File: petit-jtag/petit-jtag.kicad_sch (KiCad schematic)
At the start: 9 parts, among them CON101 JTAG-2X3-1.27MM-HDR, CON102 USB-B1HSB6, CON103 JTAG-2X5-HDR-SHROUD, CON104 HDR1X3, U101 AZ1117CH-3.3TRG1

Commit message: mostly done v1.0
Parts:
- logo101: footprint db-artwork:db-logo_10mm -> db-artwork:db-logo_7.5mm
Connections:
- net +3V3: now also CON103.4 (Vcc)
- net VCC: no longer CON103.4 (Vcc)
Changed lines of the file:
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@@
   (junction (at 221.615 81.28) (diameter 0) (color 0 0 0 0)
   )
-  (junction (at 224.155 73.66) (diameter 0) (color 0 0 0 0)
-  )
   (junction (at 92.075 95.25) (diameter 0) (color 0 0 0 0)
   )
@@
     (stroke (width 0) (type default))
   )
-  (wire (pts (xy 224.155 94.615) (xy 224.155 73.66))
-    (stroke (width 0) (type default))
-  )
   (wire (pts (xy 190.5 102.235) (xy 198.755 102.235))
     (stroke (width 0) (type default))
@@
     (stroke (width 0) (type default))
   )
-  (wire (pts (xy 224.155 73.66) (xy 225.425 73.66))
+  (wire (pts (xy 217.805 73.66) (xy 225.425 73.66))
     (stroke (width 0) (type default))
   )
@@
   )
   (wire (pts (xy 221.615 97.155) (xy 221.615 81.28))
-    (stroke (width 0) (type default))
-  )
-  (wire (pts (xy 217.805 73.66) (xy 224.155 73.66))
     (stroke (width 0) (type default))
   )
@@
     (effects (font (size 1.27 1.27)) (justify left bottom))
   )
-  (symbol (lib_id "power:+3V3") (at 129.54 70.485 0) (unit 1)
-    (in_bom yes) (on_board yes) (dnp no) (fields_autoplaced)
-    (property "Reference" "#PWR0102" (at 129.54 74.295 0)
-      (effects (font (size 1.27 1.27)) hide)
-    )
-    (property "Value" "+3V3" (at 129.54 66.04 0)
-      (effects (font (size 1.27 1.27)))
-    )
-    (property "Footprint" "" (at 129.54 70.485 0)
-      (effects (font (size 1.27 1.27)) hide)
-    )
-    (property "Datasheet" "" (at 129.54 70.485 0)
+  (symbol (lib_id "power:+3V3") (at 225.425 73.66 270) (unit 1)
+    (in_bom yes) (on_board yes) (dnp no) (fields_autoplaced)
+    (property "Reference" "#PWR0102" (at 221.615 73.66 0)
+      (effects (font (size 1.27 1.27)) hide)
+    )
+    (property "Value" "+3V3" (at 228.6 73.66 90)
+      (effects (font (size 1.27 1.27)) (justify left))
+    )
+    (property "Footprint" "" (at 225.425 73.66 0)
+      (effects (font (size 1.27 1.27)) hide)
+    )
+    (property "Datasheet" "" (at 225.425 73.66 0)
       (effects (font (size 1.27 1.27)) hide)
     )
@@
       (effects (font (size 1.524 1.524)) (justify left))
     )
-    (property "Footprint" "db-artwork:db-logo_10mm" (at 182.245 156.845 0)
+    (property "Footprint" "db-artwork:db-logo_7.5mm" (at 182.245 156.845 0)
       (effects (font (size 1.524 1.524)) hide)
     )
@@
         (path "/9bb394b8-bc21-4e2d-a33d-3ebd944f79a1"
           (reference "CON104") (unit 1)
+        )
+      )
+    )
+  )
+  (symbol (lib_id "power:+3V3") (at 129.54 70.485 0) (unit 1)
+    (in_bom yes) (on_board yes) (dnp no) (fields_autoplaced)
+    (property "Reference" "#PWR0108" (at 129.54 74.295 0)
+      (effects (font (size 1.27 1.27)) hide)
+    )
+    (property "Value" "+3V3" (at 129.54 66.04 0)
+      (effects (font (size 1.27 1.27)))
+    )
+    (property "Footprint" "" (at 129.54 70.485 0)
+      (effects (font (size 1.27 1.27)) hide)
+    )
+    (property "Datasheet" "" (at 129.54 70.485 0)
+      (effects (font (size 1.27 1.27)) hide)
+    )
+    (pin "1")
+    (instances
+      (project "petit-jtag"
+        (path "/9bb394b8-bc21-4e2d-a33d-3ebd944f79a1"
+          (reference "#PWR0108") (unit 1)
         )
       )
@@
     )
   )
-  (symbol (lib_id "power:VCC") (at 225.425 73.66 270) (unit 1)
-    (in_bom yes) (on_board yes) (dnp no) (fields_autoplaced)
-    (property "Reference" "#PWR0106" (at 221.615 73.66 0)
-      (effects (font (size 1.27 1.27)) hide)
-    )
-    (property "Value" "VCC" (at 228.6 73.66 90)
-      (effects (font (size 1.27 1.27)) (justify left))
-    )
-    (property "Footprint" "" (at 225.425 73.66 0)
-      (effects (font (size 1.27 1.27)) hide)
-    )
-    (property "Datasheet" "" (at 225.425 73.66 0)
-      (effects (font (size 1.27 1.27)) hide)
-    )
+  (symbol (lib_id "power:VCC") (at 224.155 94.615 270) (unit 1)
+    (in_bom yes) (on_board yes) (dnp no) (fields_autoplaced)
+    (property "Reference" "#PWR0106" (at 220.345 94.615 0)
+      (effects (font (size 1.27 1.27)) hide)
+    )
+    (property "Value" "VCC" (at 227.33 94.615 90)
+      (effects (font (size 1.27 1.27)) (justify left))
+    )
+    (property "Footprint" "" (at 224.155 94.615 0)
+      (effects (font (size 1.27 1.27)) hide)
+    )
+    (property "Datasheet" "" (at 224.155 94.615 0)
+      (effects (font (size 1.27 1.27)) hide)
+    )

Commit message: version 1.0 ready
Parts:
- added CON105: HDR1X2, db-thparts:HDR1X2, symbol db-connectors:HDR1X2
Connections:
- net +5V: now also CON105.1
- net GND: now also CON105.2

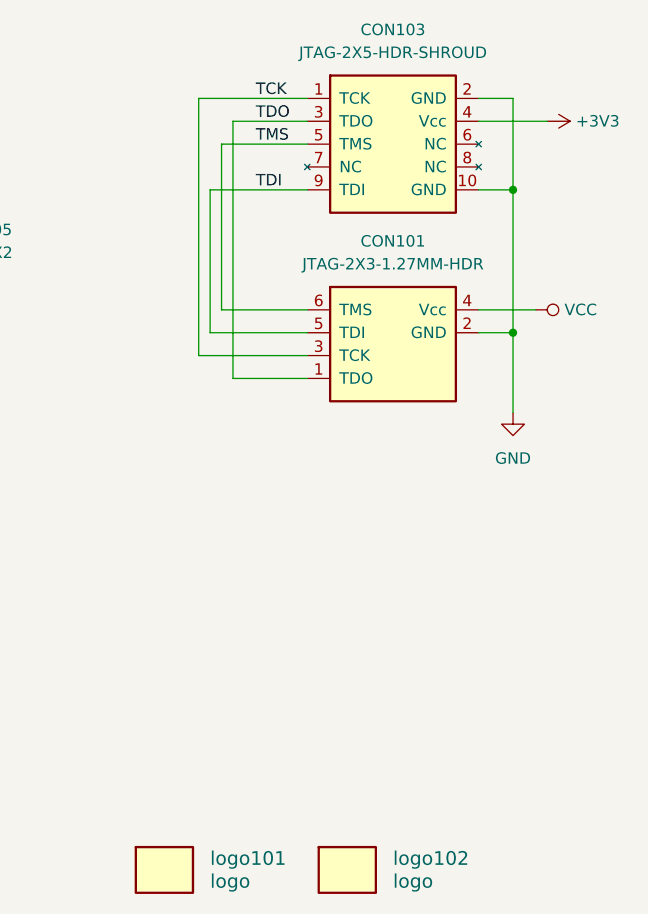
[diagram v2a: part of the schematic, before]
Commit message: updated with new staggered pin headers instead of 2x3
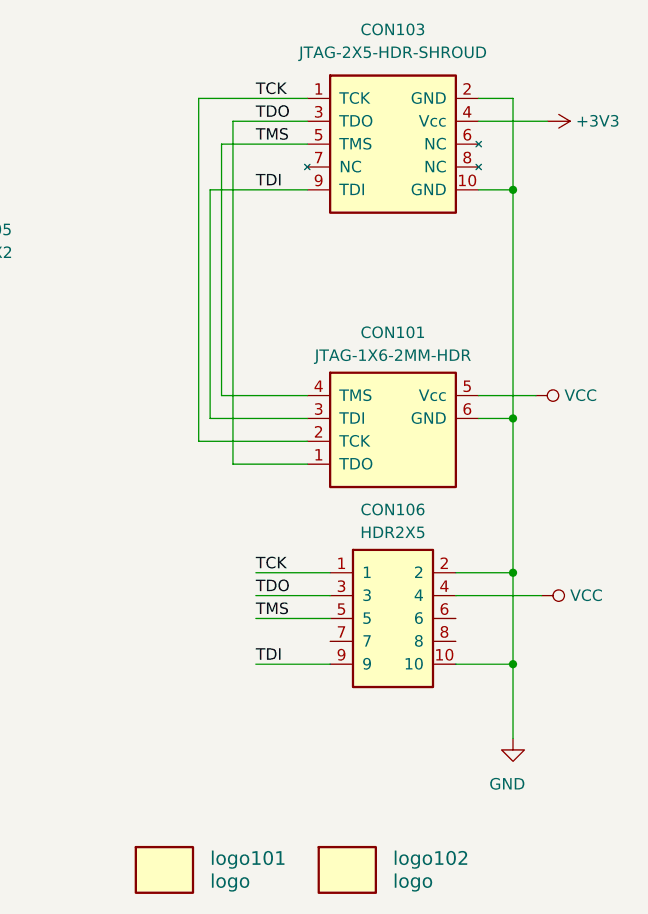
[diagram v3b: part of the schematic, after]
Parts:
- removed CON101: JTAG-2X3-1.27MM-HDR, db-thparts:HDR2X3_1.27MM, symbol db-connectors:JTAG-2X3-1.27MM-HDR
- added CON101: JTAG-1X6-2MM-HDR, db-thparts:HDR1X6_2MM, symbol db-connectors:JTAG-1X6-2MM-HDR
- added CON106: HDR2X5, db-thparts:HDR2X5-JTAG, symbol db-connectors:HDR2X5
- logo102: footprint db-artwork:oshw-logo_7.5mm -> db-artwork:oshw-logo_5mm
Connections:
- net GND: now also CON101.6 (GND), CON106.10, CON106.2
- net TCK: now also CON101.2 (TCK), CON106.1
- net TDI: now also CON101.3 (TDI), CON106.9
- net TDO: now also CON101.1 (TDO), CON106.3
- net TMS: now also CON101.4 (TMS), CON106.5
- net VCC: now also CON101.5 (Vcc), CON106.4

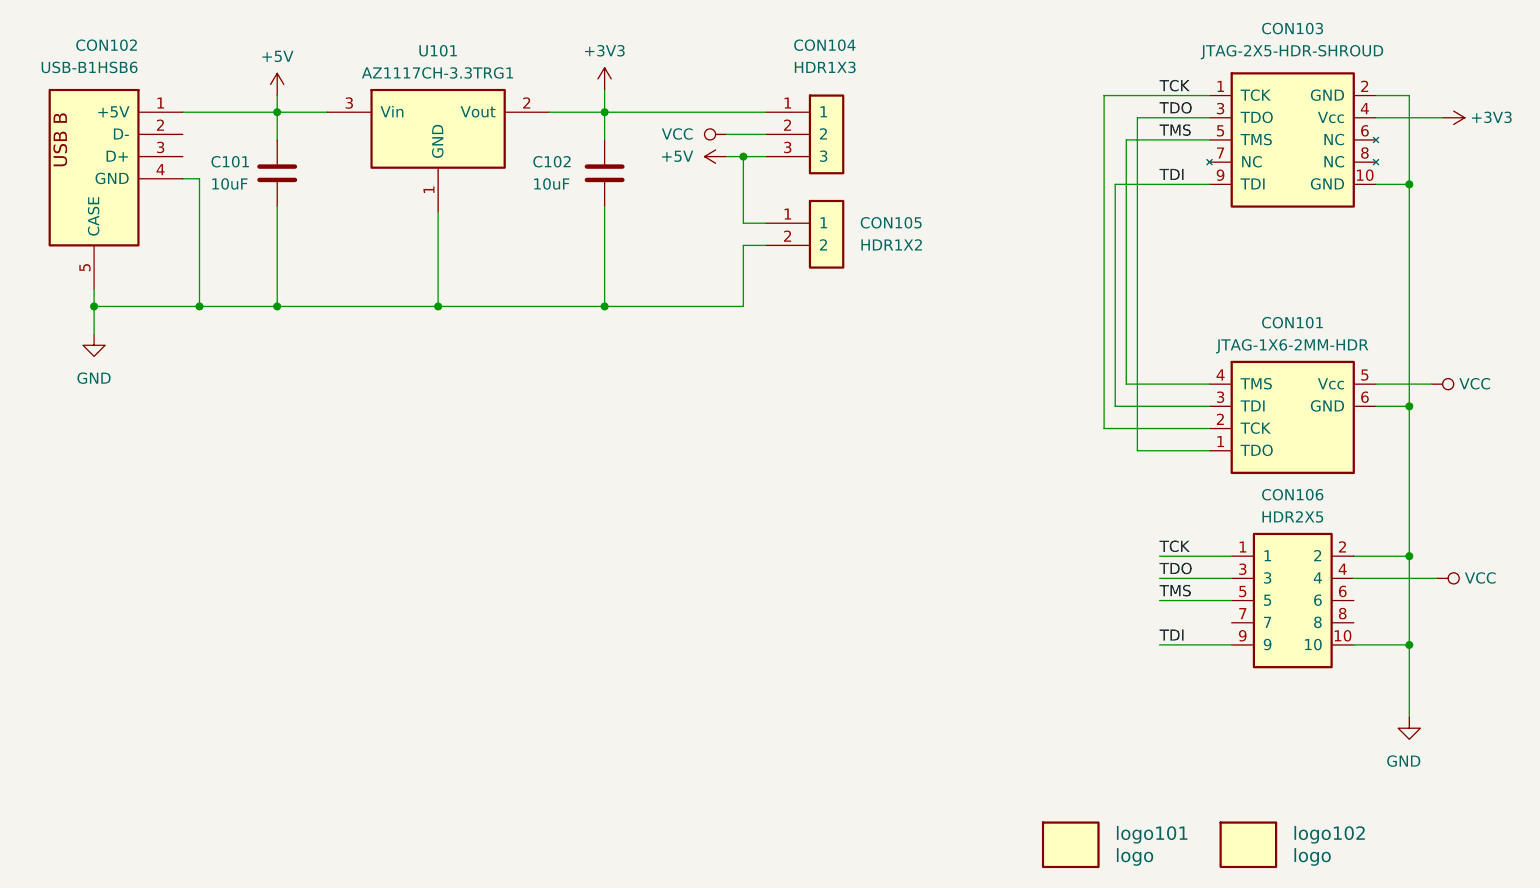
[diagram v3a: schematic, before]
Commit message: swd v1.0 sch complete, jtag v1.1 files
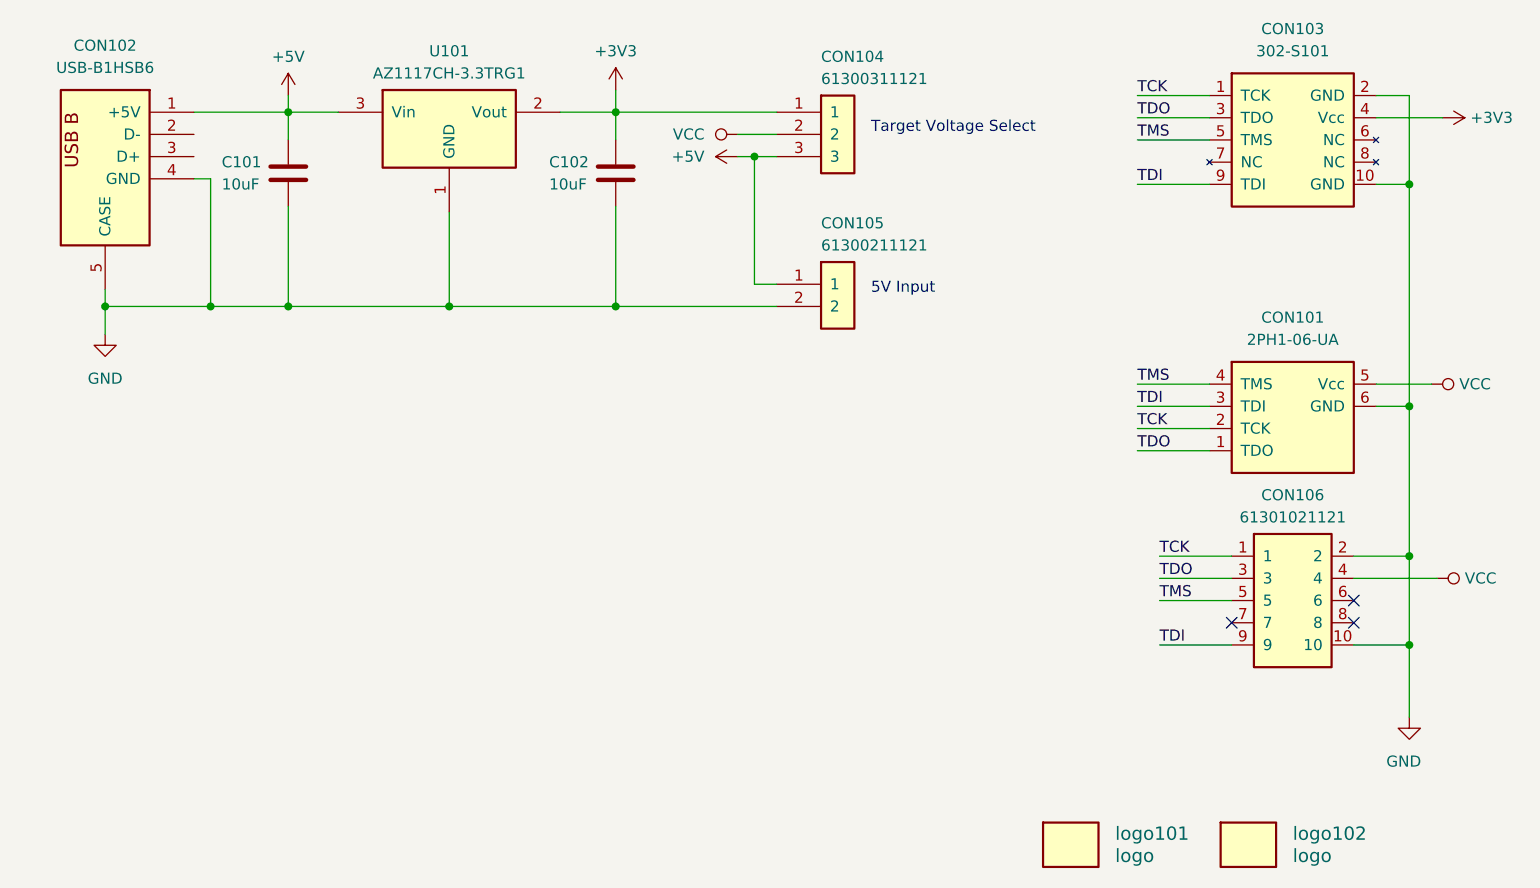
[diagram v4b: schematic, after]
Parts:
- C101, C102: Digikey 1276-1096-1-ND -> (none); Supplier (none) -> www.digikey.ca; Supplier Number (none) -> 1276-1096-1-ND
- CON101: value JTAG-1X6-2MM-HDR -> 2PH1-06-UA; Part Number 2057-2PH1-06-UA-ND -> (none); Supplier Number (none) -> 2057-2PH1-06-UA-ND
- CON102: Digikey ED2983-ND -> (none); Supplier (none) -> www.digikey.ca; Supplier Number (none) -> ED2983-ND
- CON103: value JTAG-2X5-HDR-SHROUD -> 302-S101; Digikey ED1543-ND -> (none); Supplier (none) -> www.digikey.ca; Supplier Number (none) -> ED1543-ND
- CON104: value HDR1X3 -> 61300311121; Digikey 732-5316-ND -> (none); Supplier (none) -> www.digikey.ca; Supplier Number (none) -> 732-5316-ND
- CON105: value HDR1X2 -> 61300211121; Digikey 952-2262-ND -> (none); Supplier (none) -> www.digikey.ca; Supplier Number (none) -> 732-5315-ND
- CON106: value HDR2X5 -> 61301021121; Digikey ED1543-ND -> (none); Supplier (none) -> www.digikey.ca; Supplier Number (none) -> 732-2672-ND
- logo101, logo102: now left out of the parts list
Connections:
- no-connect marks 0 -> 3
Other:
- note added: "5V Input"
- note added: "Target Voltage Select"
- moved on the sheet: C101

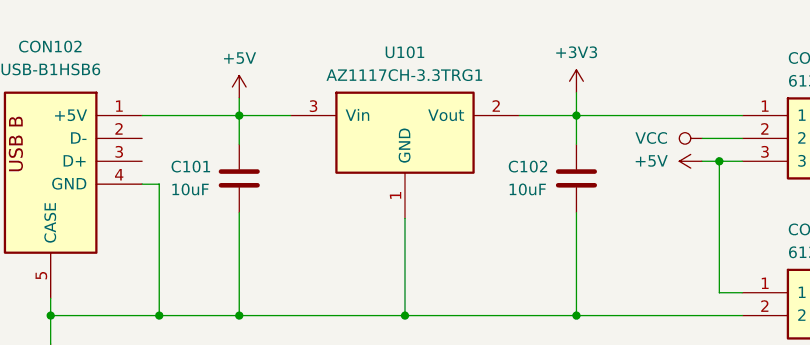
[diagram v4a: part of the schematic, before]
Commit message: separate petit-swd into its own repo
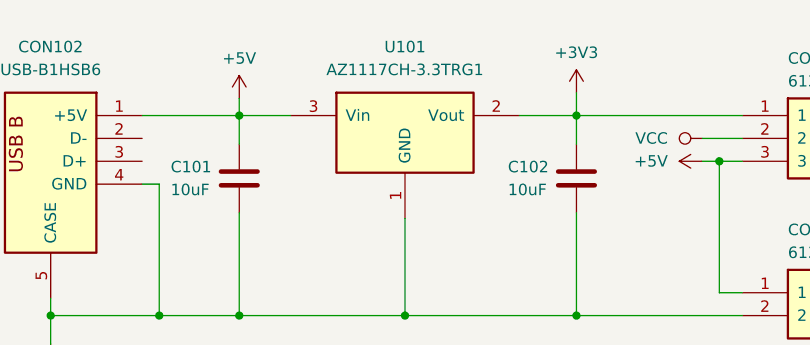
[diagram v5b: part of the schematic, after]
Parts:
- U101: Digikey AZ1117CH-3.3TRG1DICT-ND -> (none); Reviewed 2019-03-19 -> (none); Supplier (none) -> www.digikey.ca; Supplier Number (none) -> AZ1117CH-3.3TRG1DICT-ND
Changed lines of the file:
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@@
+    )
+  )
+  (symbol (lib_name "AZ1117CH-3.3TRG1_1") (lib_id "db-sem:AZ1117CH-3.3TRG1") (at 104.14 70.485 0) (unit 1)
+    (in_bom yes) (on_board yes) (dnp no) (fields_autoplaced)
+    (property "Reference" "U101" (at 111.76 65.405 0)
+      (effects (font (size 1.27 1.27)))
+    )
+    (property "Value" "AZ1117CH-3.3TRG1" (at 111.76 67.945 0)
+      (effects (font (size 1.27 1.27)))
+    )
+    (property "Footprint" "db-smt:SOT-223" (at 120.015 63.5 0)
+      (effects (font (size 1.524 1.524)) hide)
+    )
+    (property "Datasheet" "https://www.diodes.com/assets/Datasheets/AZ1117C.pdf" (at 133.35 60.96 0)
+      (effects (font (size 1.524 1.524)) hide)
+    )
+    (property "Supplier" "www.digikey.ca" (at 114.3 51.435 0)
+      (effects (font (size 1.27 1.27)) hide)
+    )
+    (property "Supplier Number" "AZ1117CH-3.3TRG1DICT-ND" (at 121.92 59.055 0)
+      (effects (font (size 1.524 1.524)) hide)
+    )
+    (property "Description" "IC REG LINEAR 3.3V 800MA SOT223" (at 125.73 55.88 0)
+      (effects (font (size 1.524 1.524)) hide)
+    )
+    (pin "1")
+    (pin "2")
+    (pin "3")
+    (instances
+      (project "petit-jtag"
+        (path "/9bb394b8-bc21-4e2d-a33d-3ebd944f79a1"
+          (reference "U101") (unit 1)
+        )
+      )
     )
   )
@@
         )
       )
-    )
-  )
-  (symbol (lib_id "db-sem:AZ1117CH-3.3TRG1") (at 104.14 70.485 0) (unit 1)
-    (in_bom yes) (on_board yes) (dnp no) (fields_autoplaced)
-    (property "Reference" "U101" (at 111.76 66.04 0)
-      (effects (font (size 1.27 1.27)))
-    )
-    (property "Value" "AZ1117CH-3.3TRG1" (at 111.76 68.58 0)
-      (effects (font (size 1.27 1.27)))
-    )
-    (property "Footprint" "db-smt:SOT-223" (at 120.015 63.5 0)
-      (effects (font (size 1.524 1.524)) hide)
-    )
-    (property "Datasheet" "https://www.diodes.com/assets/Datasheets/AZ1117C.pdf" (at 133.35 60.96 0)
-      (effects (font (size 1.524 1.524)) hide)
-    )
-    (property "Digikey" "AZ1117CH-3.3TRG1DICT-ND" (at 121.92 59.055 0)
-      (effects (font (size 1.524 1.524)) hide)
-    )
-    (property "Description" "IC REG LINEAR 3.3V 800MA SOT223" (at 125.73 55.88 0)
-      (effects (font (size 1.524 1.524)) hide)
-    )
-    (property "Reviewed" "2019-03-19" (at 113.03 52.705 0)
-      (effects (font (size 1.524 1.524)) hide)
-    )
-    (pin "1")
-    (pin "2")
-    (pin "3")
-    (instances
-      (project "petit-jtag"
-        (path "/9bb394b8-bc21-4e2d-a33d-3ebd944f79a1"
-          (reference "U101") (unit 1)
-        )
-      )
